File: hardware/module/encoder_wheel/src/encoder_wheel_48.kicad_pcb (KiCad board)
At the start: 2 copper layers, 74 x 74 mm, 2 parts

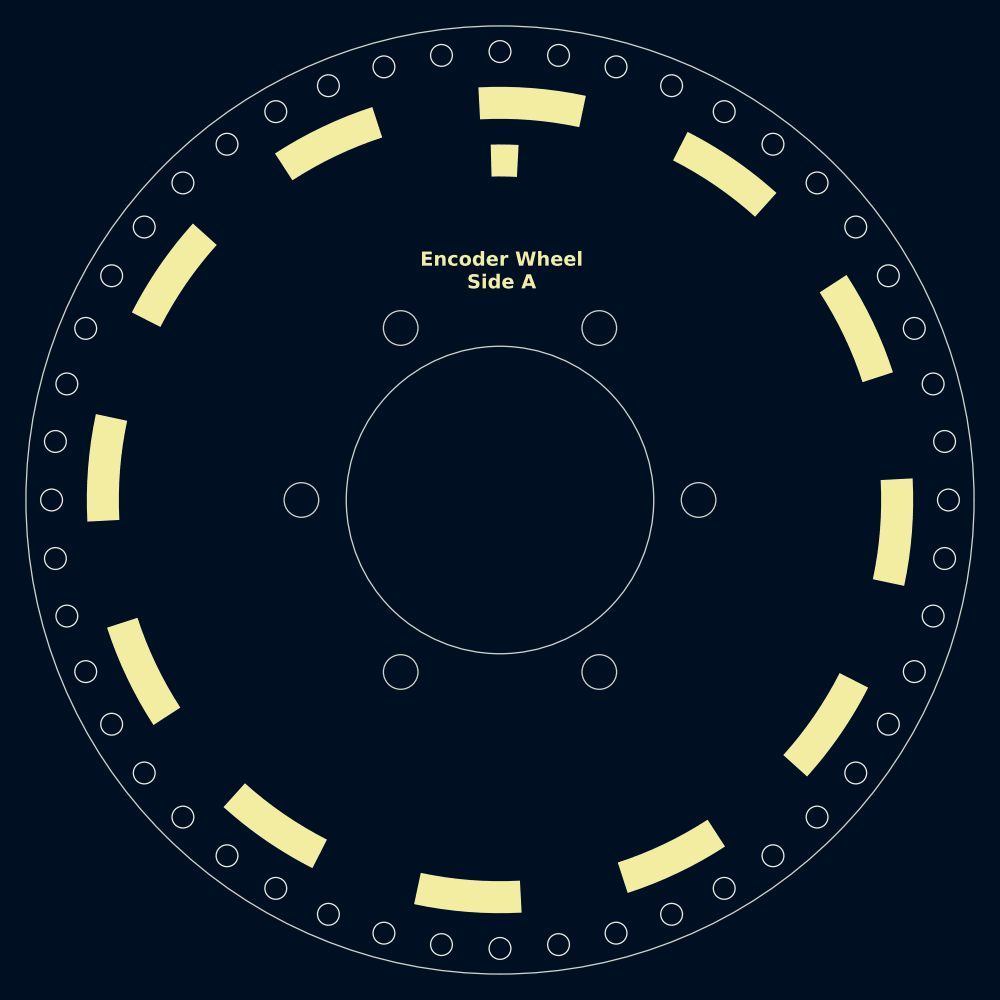
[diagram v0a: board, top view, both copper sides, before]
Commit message: Rework top connector and side panel connections to increase power rating. Switch from 2 channel to 4 channel incremental encoder.
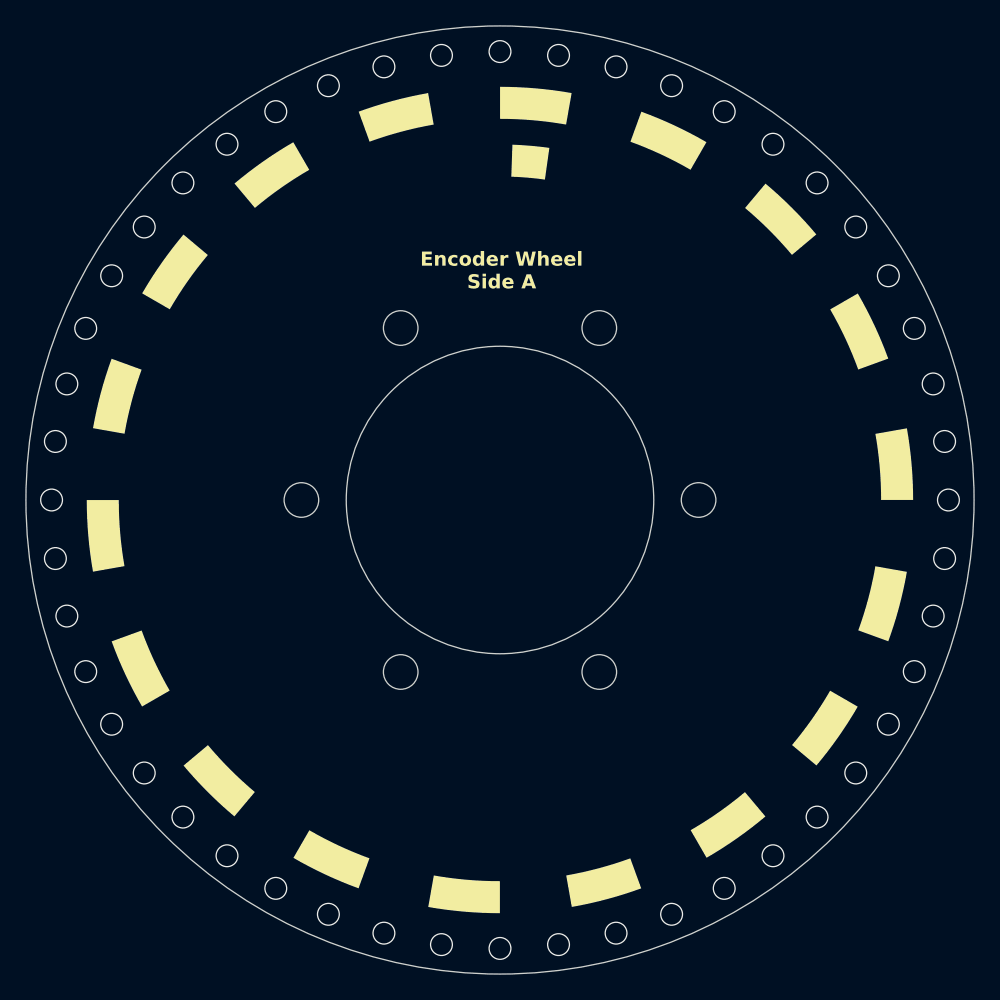
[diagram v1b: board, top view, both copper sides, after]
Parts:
- removed the REF** at (101.0, 99.9) (x2)
- added REF**: OpenFlapEncoderPattern48_18_Inc_2.5mm, EncoderPattern:OpenFlapEncoderPattern48_18_Inc_2.5mm, F.Cu at (101.0, 99.9)
- added REF**: OpenFlapEncoderPattern48_18_Inc_2.5mm, EncoderPattern:OpenFlapEncoderPattern48_18_Inc_2.5mm, B.Cu at (101.0, 99.9)
